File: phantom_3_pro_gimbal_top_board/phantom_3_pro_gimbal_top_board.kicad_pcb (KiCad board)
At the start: 2 copper layers, 67.2 x 57.3 mm, 667 parts, among them J1 CONN_CENTER, J2 CONN_ARMS2, J3 CONN_ARMS1, J4 CONN_OFDM, J5 USB_OTG, J7 CONN_MOTOR, J8 Micro_SD_Card, Q1 PMBT3904, U1 TMS320DM365ZCE, U10 LM26480, U11 TPS650061, U12 MLX90316, U13 NCP585, U14 TS3USB221A-Q1, U15 TS3USB221A-Q1, U16 dsPIC33EP128MC504, U2 STM32F407IGH6, U3 MT29F1G08, U4 MT29F2G08, U5 IS43DR16640B, U6 TLV62130, U7 SN74AVC8T245RHL, U8 EDB8132B3PB, U9 TLV62130

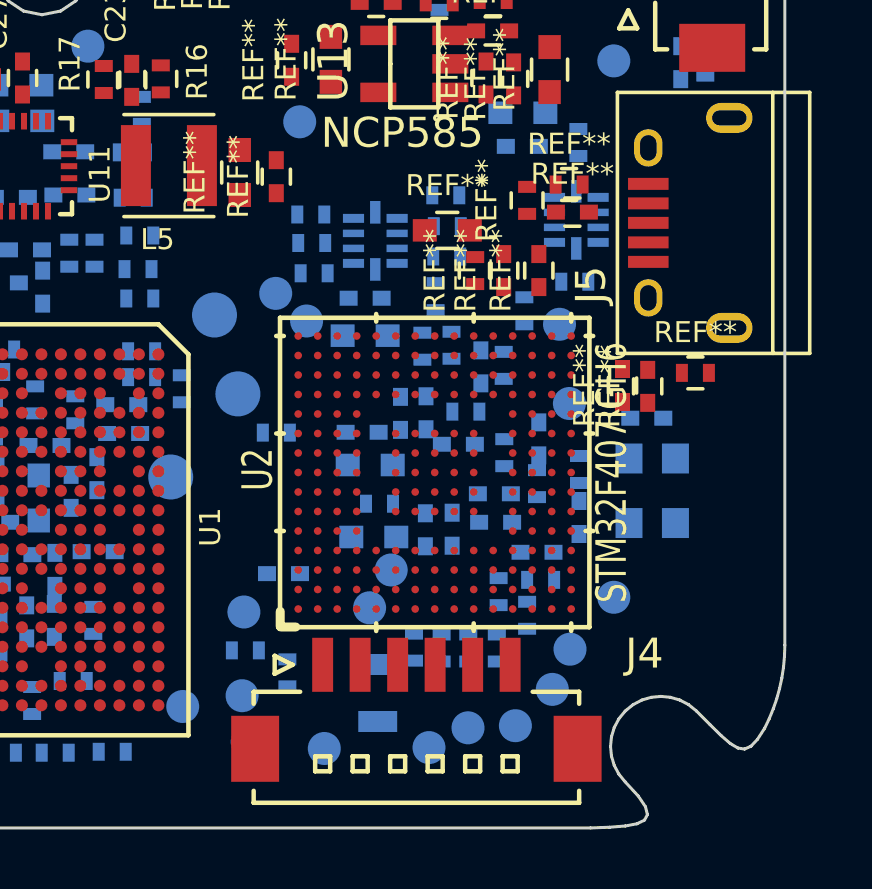
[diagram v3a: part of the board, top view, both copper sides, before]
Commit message: Gimbal Top: Drawn USB circuits, and USB mux'es.
USB multiplexers are used for both USB outputs, though
connected in very different ways.
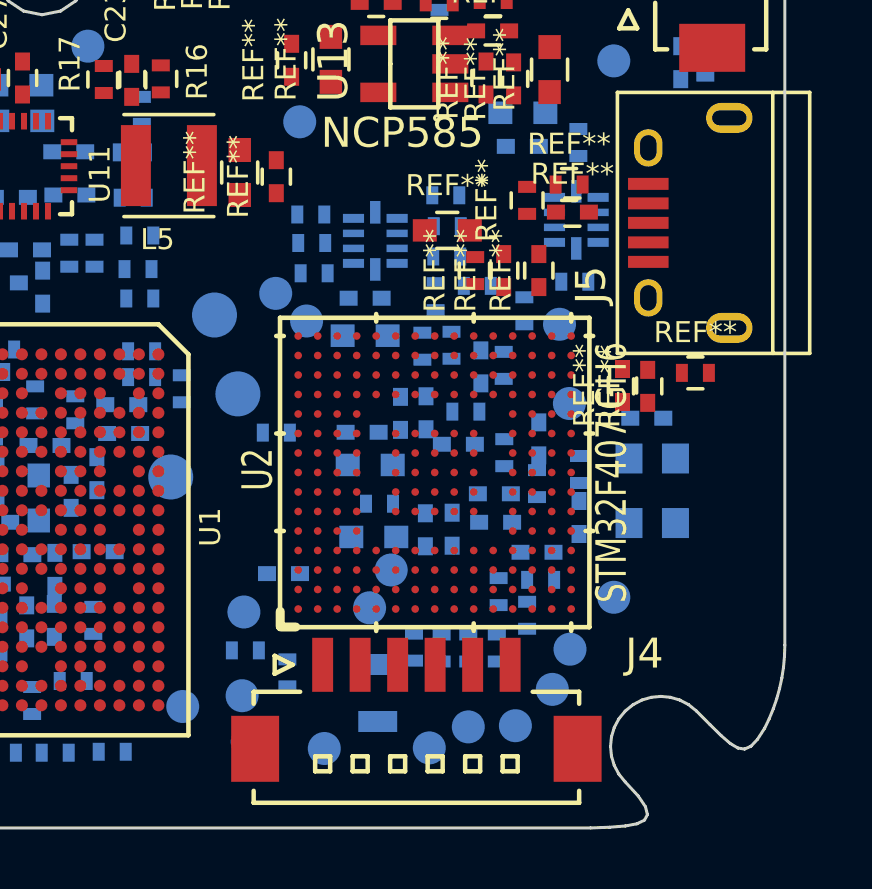
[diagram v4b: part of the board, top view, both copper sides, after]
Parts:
- added R34: ∞Ω, Resistors_SMD:R_0402, B.Cu at (69.7, 52.0)
- R29, R31, R32, R33: renamed from REF**; value R_0402 -> 0Ω
- R35, R36: renamed from REF**; value R_0402 -> 4.7kΩ
- moved TP35 1.48 mm to (69.4, 66.7)
- moved TP49 1.45 mm to (68.1, 67.4)
- turned R29 to 180 degrees
- turned R31 to 180 degrees
- turned R32 to 180 degrees
- turned R33 to 180 degrees
- turned R35 to 180 degrees
- turned U14 to 180 degrees
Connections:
- J4 pad 3: Net-(J4-Pad3) -> GND
- R29 pad 1: (no net) -> Net-(J4-Pad1)
- R29 pad 2: (no net) -> Net-(R29-Pad2)
- R31 pad 1: (no net) -> Net-(J4-Pad2)
- R31 pad 2: (no net) -> Net-(R31-Pad2)
- R32 pad 1: (no net) -> Net-(R28-Pad2)
- R32 pad 2: (no net) -> Net-(R32-Pad2)
- R33 pad 1: (no net) -> Net-(R30-Pad2)
- R33 pad 2: (no net) -> Net-(R33-Pad2)
- R35 pad 1: (no net) -> GND
- R35 pad 2: (no net) -> Net-(R35-Pad2)
- R36 pad 1: (no net) -> GND
- R36 pad 2: (no net) -> Net-(R34-Pad2)
- TP34 pad 1: Net-(TP34-Pad1) -> Net-(J4-Pad6)
- TP35 pad 1: Net-(TP35-Pad1) -> Net-(J4-Pad5)
- TP36 pad 1: Net-(TP36-Pad1) -> /3.3VD
- U14 pad 10: Net-(U14-Pad10) -> /3.3VD
- U14 pad 3: Net-(U14-Pad3) -> Net-(J5-Pad3)
- U14 pad 4: Net-(U14-Pad4) -> Net-(J5-Pad2)
- U14 pad 5: Net-(U14-Pad5) -> GND
- U15 pad 1: Net-(U15-Pad1) -> Net-(TP8-Pad1)
- U15 pad 10: Net-(U15-Pad10) -> /3.3VD
- U15 pad 2: Net-(U15-Pad2) -> Net-(TP7-Pad1)
- U15 pad 3: Net-(U15-Pad3) -> Net-(R28-Pad2)
- U15 pad 4: Net-(U15-Pad4) -> Net-(R30-Pad2)
- U15 pad 5: Net-(U15-Pad5) -> GND
- U15 pad 6: Net-(U15-Pad6) -> Net-(R35-Pad2)
- U15 pad 7: Net-(U15-Pad7) -> Net-(R29-Pad2)
- U15 pad 8: Net-(U15-Pad8) -> Net-(R31-Pad2)
- U15 pad 9: Net-(U15-Pad9) -> Net-(R34-Pad2)
